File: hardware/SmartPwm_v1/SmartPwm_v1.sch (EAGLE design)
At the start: 41 parts, among them IC1 7805T, J1 ESP32-PICO-KIT, Q1 IRF3704-H, Q2 IRF3704-H, Q3 IRF3704-H, Q4 IRF3704-H, U1 ICL7667CBAZA, U3 ICL7667CBAZA

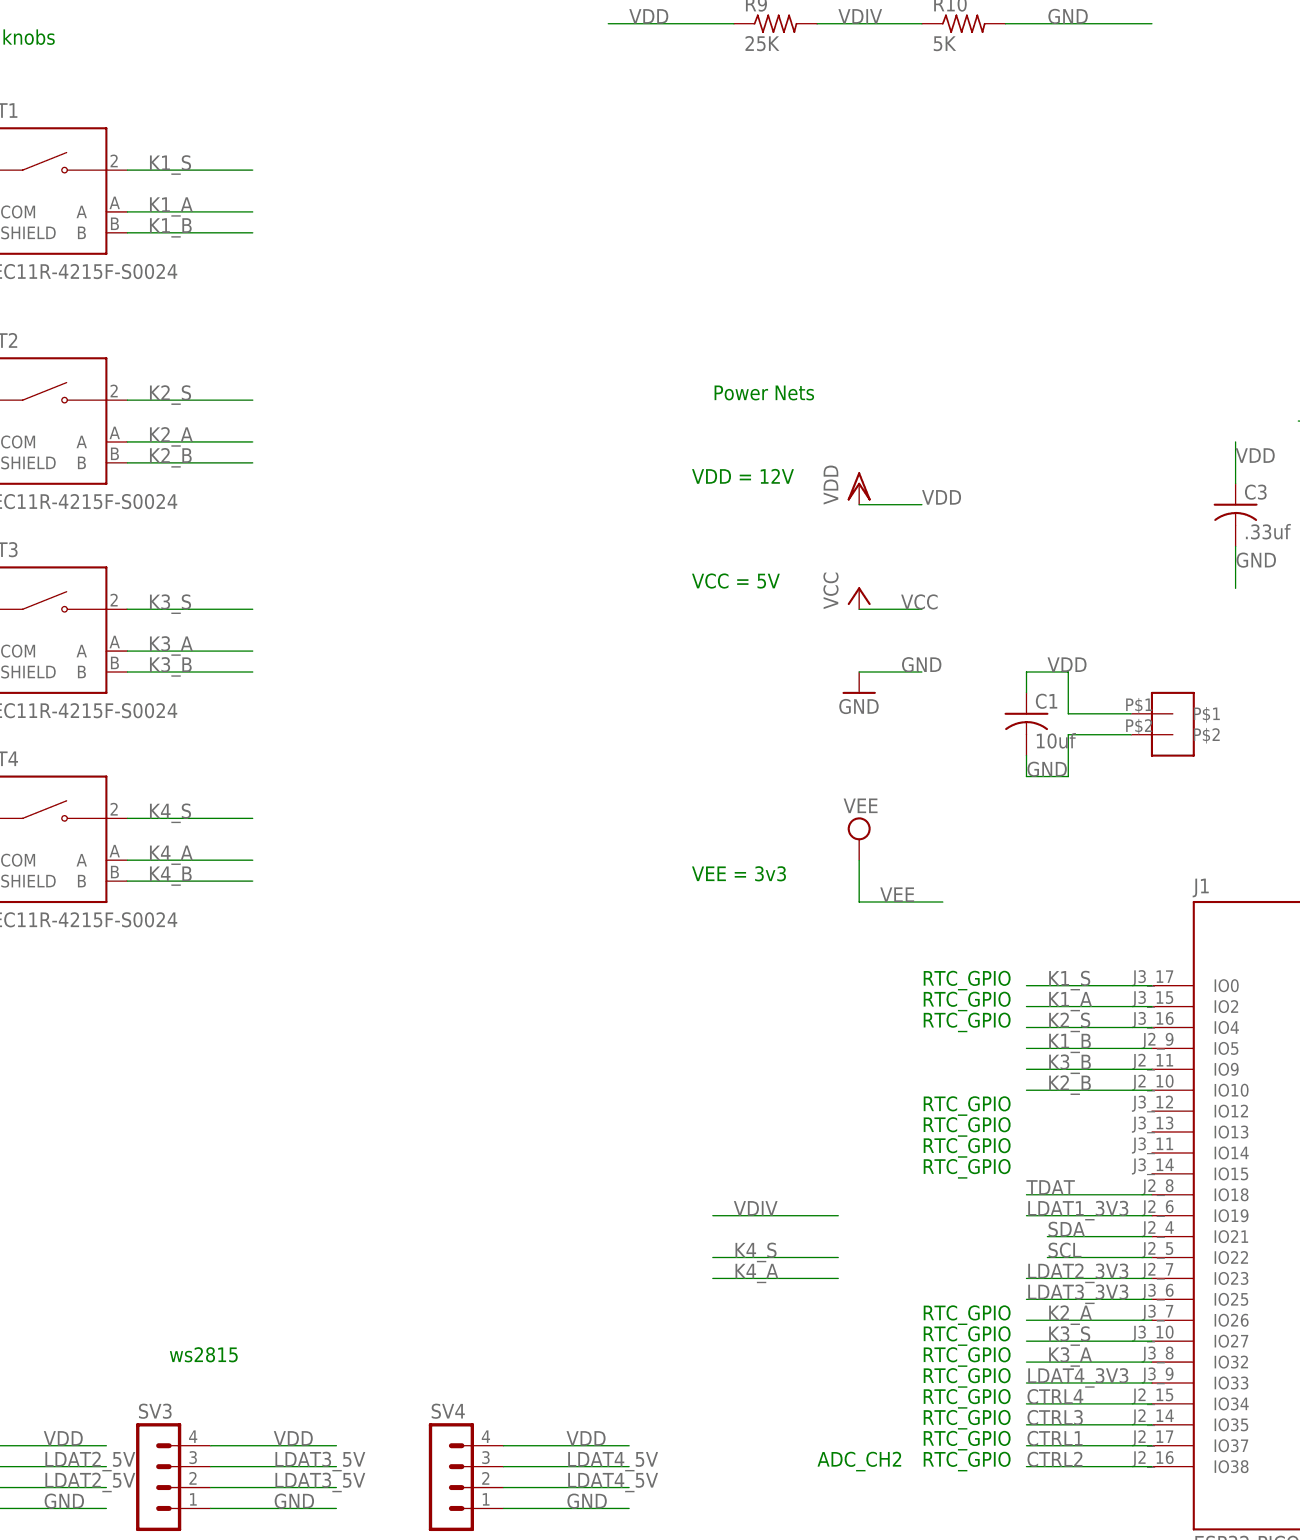
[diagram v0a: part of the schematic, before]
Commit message: rewire gpios, preliminary routing
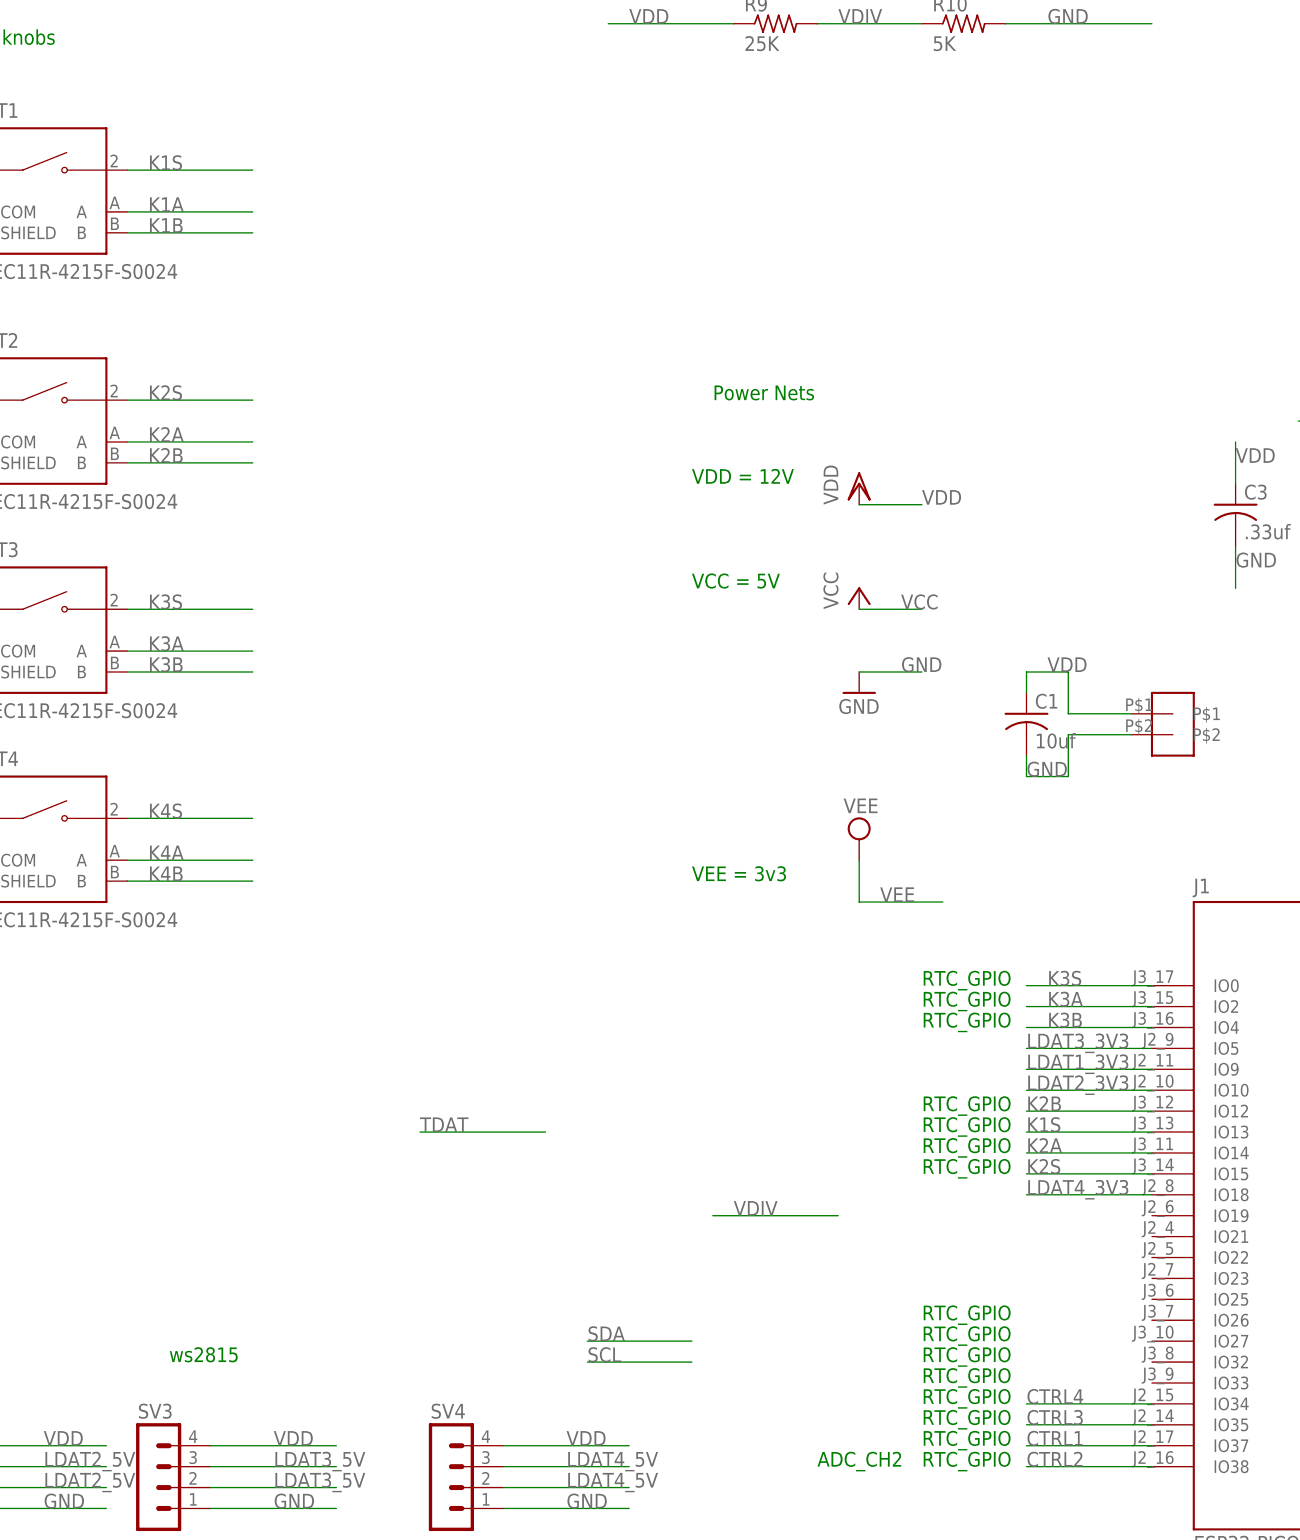
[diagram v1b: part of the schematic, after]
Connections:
- net K4_A renamed K4A
- net K4_B renamed K4B
- net K4_S renamed K4S
- removed net K1_A: J1.IO2, MT1.A
- removed net K1_B: J1.IO5, MT1.B
- removed net K1_S: J1.IO0, MT1.2
- removed net K2_A: J1.IO26, MT2.A
- removed net K2_B: J1.IO10, MT2.B
- removed net K2_S: J1.IO4, MT2.2
- removed net K3_A: J1.IO32, MT3.A
- removed net K3_B: J1.IO9, MT3.B
- removed net K3_S: J1.IO27, MT3.2
- new net K1A: MT1.A
- new net K1B: MT1.B
- new net K1S: J1.IO13, MT1.2
- new net K2A: J1.IO14, MT2.A
- new net K2B: J1.IO12, MT2.B
- new net K2S: J1.IO15, MT2.2
- new net K3A: J1.IO2, MT3.A
- new net K3B: J1.IO4, MT3.B
- new net K3S: J1.IO0, MT3.2
- net LDAT1_3V3: now also J1.IO9; no longer J1.IO19
- net LDAT2_3V3: now also J1.IO10; no longer J1.IO23
- net LDAT3_3V3: now also J1.IO5; no longer J1.IO25
- net LDAT4_3V3: now also J1.IO18; no longer J1.IO33
- net SCL: no longer J1.IO22
- net SDA: no longer J1.IO21
- net TDAT: no longer J1.IO18
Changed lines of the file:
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@@
 <net name="SCL" class="0">
-<segment>
-<pinref part="J1" gate="G$1" pin="IO22"/>
-<wire x1="50.8" y1="-20.32" x2="38.1" y2="-20.32" width="0.1524" layer="91"/>
-<label x="38.1" y="-20.32" size="1.778" layer="95"/>
-</segment>
 <segment>
 <wire x1="58.42" y1="-71.12" x2="66.04" y2="-71.12" width="0.1524" layer="91"/>
@@
 <pinref part="SV5" gate="1" pin="4"/>
 </segment>
+<segment>
+<wire x1="-5.08" y1="-33.02" x2="-17.78" y2="-33.02" width="0.1524" layer="91"/>
+<label x="-17.78" y="-33.02" size="1.778" layer="95"/>
+</segment>
 </net>
 <net name="SDA" class="0">
-<segment>
-<pinref part="J1" gate="G$1" pin="IO21"/>
-<wire x1="50.8" y1="-17.78" x2="38.1" y2="-17.78" width="0.1524" layer="91"/>
-<label x="38.1" y="-17.78" size="1.778" layer="95"/>
-</segment>
 <segment>
 <wire x1="58.42" y1="-78.74" x2="66.04" y2="-78.74" width="0.1524" layer="91"/>
@@
 <label x="45.72" y="-91.44" size="1.778" layer="95"/>
 <pinref part="SV5" gate="1" pin="3"/>
+</segment>
+<segment>
+<wire x1="-5.08" y1="-30.48" x2="-17.78" y2="-30.48" width="0.1524" layer="91"/>
+<label x="-17.78" y="-30.48" size="1.778" layer="95"/>
 </segment>
 </net>
@@
 </segment>
 <segment>
-<pinref part="J1" gate="G$1" pin="IO18"/>
-<wire x1="50.8" y1="-12.7" x2="35.56" y2="-12.7" width="0.1524" layer="91"/>
-<label x="35.56" y="-12.7" size="1.778" layer="95"/>
-</segment>
-</net>
-<net name="K1_S" class="0">
+<wire x1="-22.86" y1="-5.08" x2="-38.1" y2="-5.08" width="0.1524" layer="91"/>
+<label x="-38.1" y="-5.08" size="1.778" layer="95"/>
+</segment>
+</net>
+<net name="K1S" class="0">
 <segment>
 <pinref part="MT1" gate="G$1" pin="2"/>
@@
 </segment>
 <segment>
-<wire x1="35.56" y1="12.7" x2="50.8" y2="12.7" width="0.1524" layer="91"/>
-<label x="38.1" y="12.7" size="1.778" layer="95"/>
-<pinref part="J1" gate="G$1" pin="IO0"/>
-</segment>
-</net>
-<net name="K1_A" class="0">
-<segment>
-<pinref part="MT1" gate="G$1" pin="A"/>
-<wire x1="-73.66" y1="106.68" x2="-58.42" y2="106.68" width="0.1524" layer="91"/>
-<label x="-71.12" y="106.68" size="1.778" layer="95"/>
-</segment>
-<segment>
-<wire x1="35.56" y1="10.16" x2="50.8" y2="10.16" width="0.1524" layer="91"/>
-<label x="38.1" y="10.16" size="1.778" layer="95"/>
-<pinref part="J1" gate="G$1" pin="IO2"/>
-</segment>
-</net>
-<net name="K1_B" class="0">
+<pinref part="J1" gate="G$1" pin="IO13"/>
+<wire x1="50.8" y1="-5.08" x2="35.56" y2="-5.08" width="0.1524" layer="91"/>
+<label x="35.56" y="-5.08" size="1.778" layer="95"/>
+</segment>
+</net>
+<net name="K1B" class="0">
 <segment>
 <pinref part="MT1" gate="G$1" pin="B"/>
@@
 <label x="-71.12" y="104.14" size="1.778" layer="95"/>
 </segment>
-<segment>
-<wire x1="35.56" y1="5.08" x2="50.8" y2="5.08" width="0.1524" layer="91"/>
-<label x="38.1" y="5.08" size="1.778" layer="95"/>
-<pinref part="J1" gate="G$1" pin="IO5"/>
-</segment>
-</net>
-<net name="K4_S" class="0">
+</net>
+<net name="K4S" class="0">
 <segment>
 <wire x1="-73.66" y1="33.02" x2="-58.42" y2="33.02" width="0.1524" layer="91"/>
@@
 <pinref part="MT4" gate="G$1" pin="2"/>
 </segment>
-<segment>
-<wire x1="-2.54" y1="-20.32" x2="12.7" y2="-20.32" width="0.1524" layer="91"/>
-<label x="0" y="-20.32" size="1.778" layer="95"/>
-</segment>
-</net>
-<net name="K4_A" class="0">
+</net>
+<net name="K4A" class="0">
 <segment>
 <wire x1="-73.66" y1="27.94" x2="-58.42" y2="27.94" width="0.1524" layer="91"/>
@@
 <pinref part="MT4" gate="G$1" pin="A"/>
 </segment>
-<segment>
-<wire x1="-2.54" y1="-22.86" x2="12.7" y2="-22.86" width="0.1524" layer="91"/>
-<label x="0" y="-22.86" size="1.778" layer="95"/>
-</segment>
-</net>
-<net name="K4_B" class="0">
+</net>
+<net name="K4B" class="0">
 <segment>
 <wire x1="-73.66" y1="25.4" x2="-58.42" y2="25.4" width="0.1524" layer="91"/>
@@
 </segment>
 </net>
-<net name="K3_B" class="0">
-<segment>
-<wire x1="-73.66" y1="50.8" x2="-58.42" y2="50.8" width="0.1524" layer="91"/>
-<label x="-71.12" y="50.8" size="1.778" layer="95"/>
-<pinref part="MT3" gate="G$1" pin="B"/>
-</segment>
-<segment>
-<wire x1="35.56" y1="2.54" x2="50.8" y2="2.54" width="0.1524" layer="91"/>
-<label x="38.1" y="2.54" size="1.778" layer="95"/>
-<pinref part="J1" gate="G$1" pin="IO9"/>
-</segment>
-</net>
-<net name="K3_A" class="0">
-<segment>
-<wire x1="-73.66" y1="53.34" x2="-58.42" y2="53.34" width="0.1524" layer="91"/>
-<label x="-71.12" y="53.34" size="1.778" layer="95"/>
-<pinref part="MT3" gate="G$1" pin="A"/>
-</segment>
-<segment>
-<wire x1="35.56" y1="-33.02" x2="50.8" y2="-33.02" width="0.1524" layer="91"/>
-<label x="38.1" y="-33.02" size="1.778" layer="95"/>
-<pinref part="J1" gate="G$1" pin="IO32"/>
-</segment>
-</net>
-<net name="K3_S" class="0">
-<segment>
-<wire x1="-73.66" y1="58.42" x2="-58.42" y2="58.42" width="0.1524" layer="91"/>
-<label x="-71.12" y="58.42" size="1.778" layer="95"/>
-<pinref part="MT3" gate="G$1" pin="2"/>
-</segment>
-<segment>
-<wire x1="35.56" y1="-30.48" x2="50.8" y2="-30.48" width="0.1524" layer="91"/>
-<label x="38.1" y="-30.48" size="1.778" layer="95"/>
-<pinref part="J1" gate="G$1" pin="IO27"/>
-</segment>
-</net>
-<net name="K2_B" class="0">
+<net name="K2B" class="0">
 <segment>
 <wire x1="-73.66" y1="76.2" x2="-58.42" y2="76.2" width="0.1524" layer="91"/>
@@
 </segment>
 <segment>
-<wire x1="35.56" y1="0" x2="50.8" y2="0" width="0.1524" layer="91"/>
-<label x="38.1" y="0" size="1.778" layer="95"/>
-<pinref part="J1" gate="G$1" pin="IO10"/>
-</segment>
-</net>
-<net name="K2_A" class="0">
+<pinref part="J1" gate="G$1" pin="IO12"/>
+<wire x1="50.8" y1="-2.54" x2="35.56" y2="-2.54" width="0.1524" layer="91"/>
+<label x="35.56" y="-2.54" size="1.778" layer="95"/>
+</segment>
+</net>
+<net name="K2A" class="0">
 <segment>
 <wire x1="-73.66" y1="78.74" x2="-58.42" y2="78.74" width="0.1524" layer="91"/>
@@
 </segment>
 <segment>
-<wire x1="35.56" y1="-27.94" x2="50.8" y2="-27.94" width="0.1524" layer="91"/>
-<label x="38.1" y="-27.94" size="1.778" layer="95"/>
-<pinref part="J1" gate="G$1" pin="IO26"/>
-</segment>
-</net>
-<net name="K2_S" class="0">
+<pinref part="J1" gate="G$1" pin="IO14"/>
+<wire x1="50.8" y1="-7.62" x2="35.56" y2="-7.62" width="0.1524" layer="91"/>
+<label x="35.56" y="-7.62" size="1.778" layer="95"/>
+</segment>
+</net>
+<net name="K2S" class="0">
 <segment>
 <wire x1="-73.66" y1="83.82" x2="-58.42" y2="83.82" width="0.1524" layer="91"/>
@@
 </segment>
 <segment>
-<wire x1="35.56" y1="7.62" x2="50.8" y2="7.62" width="0.1524" layer="91"/>
-<label x="38.1" y="7.62" size="1.778" layer="95"/>
-<pinref part="J1" gate="G$1" pin="IO4"/>
+<pinref part="J1" gate="G$1" pin="IO15"/>
+<wire x1="50.8" y1="-10.16" x2="35.56" y2="-10.16" width="0.1524" layer="91"/>
+<label x="35.56" y="-10.16" size="1.778" layer="95"/>
 </segment>
 </net>
@@
 </segment>
 <segment>
-<wire x1="50.8" y1="-15.24" x2="35.56" y2="-15.24" width="0.1524" layer="91"/>
-<label x="35.56" y="-15.24" size="1.778" layer="95"/>
-<pinref part="J1" gate="G$1" pin="IO19"/>
+<wire x1="50.8" y1="2.54" x2="35.56" y2="2.54" width="0.1524" layer="91"/>
+<label x="35.56" y="2.54" size="1.778" layer="95"/>
+<pinref part="J1" gate="G$1" pin="IO9"/>
 </segment>
 </net>
@@
 </segment>
 <segment>
-<wire x1="50.8" y1="-22.86" x2="35.56" y2="-22.86" width="0.1524" layer="91"/>
-<label x="35.56" y="-22.86" size="1.778" layer="95"/>
-<pinref part="J1" gate="G$1" pin="IO23"/>
+<wire x1="50.8" y1="0" x2="35.56" y2="0" width="0.1524" layer="91"/>
+<label x="35.56" y="0" size="1.778" layer="95"/>
+<pinref part="J1" gate="G$1" pin="IO10"/>
 </segment>
 </net>
@@
 </segment>
 <segment>
-<wire x1="50.8" y1="-35.56" x2="35.56" y2="-35.56" width="0.1524" layer="91"/>
-<label x="35.56" y="-35.56" size="1.778" layer="95"/>
-<pinref part="J1" gate="G$1" pin="IO33"/>
+<wire x1="50.8" y1="-12.7" x2="35.56" y2="-12.7" width="0.1524" layer="91"/>
+<label x="35.56" y="-12.7" size="1.778" layer="95"/>
+<pinref part="J1" gate="G$1" pin="IO18"/>
 </segment>
 </net>
@@
 </segment>
 <segment>
-<wire x1="50.8" y1="-25.4" x2="35.56" y2="-25.4" width="0.1524" layer="91"/>
-<label x="35.56" y="-25.4" size="1.778" layer="95"/>
-<pinref part="J1" gate="G$1" pin="IO25"/>
-</segment>
-</net>
+<wire x1="50.8" y1="5.08" x2="35.56" y2="5.08" width="0.1524" layer="91"/>
+<label x="35.56" y="5.08" size="1.778" layer="95"/>
+<pinref part="J1" gate="G$1" pin="IO5"/>
+</segment>
+</net>
+<net name="K1A" class="0">
+<segment>
+<pinref part="MT1" gate="G$1" pin="A"/>
+<wire x1="-73.66" y1="106.68" x2="-58.42" y2="106.68" width="0.1524" layer="91"/>
+<label x="-71.12" y="106.68" size="1.778" layer="95"/>
+</segment>
+</net>
+<net name="K3S" class="0">
+<segment>
+<wire x1="35.56" y1="12.7" x2="50.8" y2="12.7" width="0.1524" layer="91"/>
+<label x="38.1" y="12.7" size="1.778" layer="95"/>
+<pinref part="J1" gate="G$1" pin="IO0"/>
+</segment>
+<segment>
+<wire x1="-73.66" y1="58.42" x2="-58.42" y2="58.42" width="0.1524" layer="91"/>
+<label x="-71.12" y="58.42" size="1.778" layer="95"/>
+<pinref part="MT3" gate="G$1" pin="2"/>
+</segment>
+</net>
+<net name="K3A" class="0">
+<segment>
+<wire x1="35.56" y1="10.16" x2="50.8" y2="10.16" width="0.1524" layer="91"/>
+<label x="38.1" y="10.16" size="1.778" layer="95"/>
+<pinref part="J1" gate="G$1" pin="IO2"/>
+</segment>
+<segment>
+<wire x1="-73.66" y1="53.34" x2="-58.42" y2="53.34" width="0.1524" layer="91"/>
+<label x="-71.12" y="53.34" size="1.778" layer="95"/>
+<pinref part="MT3" gate="G$1" pin="A"/>
+</segment>
+</net>
+<net name="K3B" class="0">
+<segment>
+<wire x1="35.56" y1="7.62" x2="50.8" y2="7.62" width="0.1524" layer="91"/>
+<label x="38.1" y="7.62" size="1.778" layer="95"/>
+<pinref part="J1" gate="G$1" pin="IO4"/>
+</segment>
+<segment>
+<wire x1="-73.66" y1="50.8" x2="-58.42" y2="50.8" width="0.1524" layer="91"/>
+<label x="-71.12" y="50.8" size="1.778" layer="95"/>
+<pinref part="MT3" gate="G$1" pin="B"/>
+</segment>
+</net>
